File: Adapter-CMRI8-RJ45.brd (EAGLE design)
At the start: 30.9 x 38.3 mm, 6 parts

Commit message: 2.0
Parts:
- added CON1: (no value), SPCoast:1X08_LOCK
- moved J2 0.63 mm to (27.7, 11.9)
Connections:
- removed net N$17: J1.1, J2.1, J3.1
- removed net N$18: J1.2, J2.2, J3.2
- removed net N$19: J1.3, J2.3, J3.3
- removed net N$2: JP1.1, JP2.1
- removed net N$20: J1.4, J2.4, J3.4
- removed net N$21: J1.5, J2.5, J3.5
- removed net N$22: J1.6, J2.6, J3.6
- removed net N$23: J1.7, J2.7, J3.7
- removed net N$24: J1.8, J2.8, J3.8
- removed net N$3: JP1.2, JP2.2
- new net GND: JP1.1, JP1.2, JP2.1, JP2.2
- new net L1: CON1.1, J1.1, J2.1, J3.1
- new net L2: CON1.2, J1.2, J2.2, J3.2
- new net L3: CON1.3, J1.3, J2.3, J3.3
- new net L4: CON1.4, J1.4, J2.4, J3.4
- new net L5: CON1.5, J1.5, J2.5, J3.5
- new net L6: CON1.6, J1.6, J2.6, J3.6
- new net L7: CON1.7, J1.7, J2.7, J3.7
- new net L8: CON1.8, J1.8, J2.8, J3.8
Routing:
- net N$3: track 28.8 -> 0.00 mm
- net N$2: track 28.8 -> 0.00 mm
- net N$17: track 22.9 -> 0.00 mm
- net L1: track 0.00 -> 21.4 mm
- net N$23: track 21.1 -> 0.00 mm
- net N$19: track 20.2 -> 0.00 mm
- net L7: track 0.00 -> 20.1 mm
- net N$24: track 19.9 -> 0.00 mm
- net L3: track 0.00 -> 18.9 mm
- net L8: track 0.00 -> 18.9 mm
- net N$21: track 18.9 -> 0.00 mm
- net N$18: track 18.4 -> 0.00 mm
- net L5: track 0.00 -> 17.9 mm
- net L2: track 0.00 -> 17.5 mm
- net N$22: track 17.2 -> 0.00 mm
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- added copper zone on layer 16, net GND
- removed copper zone on layer 16, net N$1
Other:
- board text added: "0.100"
- board text added: "0.156"
- board text added: "2017.04"
- board text added: "3.5mm"
- board text added: "GND"
- board text added: "SPCoast"
- board text added: "v2.0"
- board text removed: "-or-"
- board text removed: "2011-10"
- board text removed: "D35725"
- board text removed: "v1.0"

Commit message: 3.0
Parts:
- removed JP1, JP2: (no value), SparkFun:SCREWTERMINAL-3.5MM-2_LOCK
- J1: value (none) -> RJ45; device con-amp:215877-7 -> SPCoast:RJ45-NO-SHIELD
- J2: device SparkFun:SCREWTERMINAL-3.5MM-8 -> SPCoast:SCREWTERMINAL-3.5MM-8
- J3: device con-molex:KK-156-8 -> SPCoast:KK-156-8-F
- moved J1 2.54 mm to (15.3, 34.2)
- moved U$1 2.54 mm to (15.2, 36.8)
- moved J3 1.27 mm to (15.6, 6.35)
- moved CON1 1.27 mm to (24.8, 15.9)
- moved J2 0.63 mm to (27.7, 12.6)
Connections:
- removed net GND: JP1.1, JP1.2, JP2.1, JP2.2
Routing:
- net L4: track 15.6 -> 19.4 mm
- net L5: track 17.9 -> 21.7 mm
- net L3: track 18.9 -> 22.7 mm
- net L6: track 16.3 -> 20.0 mm
- net L2: track 17.5 -> 21.1 mm
- net L7: track 20.1 -> 23.7 mm
- net L1: track 21.4 -> 24.9 mm
- net L8: track 18.9 -> 22.4 mm
- removed copper zone on layer 16, net GND
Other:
- board size 30.9 x 38.3 mm -> 30.9 x 39.5 mm
- board text added: "1"
- board text added: "2017.11"
- board text added: "8"
- board text added: "RJ45"
- board text added: "v3.0"
- board text removed: "2017.04"
- board text removed: "CMRI"
- board text removed: "GND"
- board text removed: "v2.0"

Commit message: 4.0
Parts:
- removed CON1: (no value), SPCoast:1X08_LOCK
- added J4: (no value), SPCoast:SCREWTERMINAL-3.5MM-4_LOCK
- added J5: (no value), SPCoast:1X08_LOCK
- added M1, M2: MOUNTINGHOLE, SPCoast:MOUNTINGHOLE
- added R1, R2, R3, R4, R5, R6, R7, R8: (no value), SPCoast:AXIAL-0.4-RES
- U$1: value OSHW-LOGOM -> DOC-OSHW-LOGO-M; device SparkFun:OSHW-LOGO-M -> SPCoast:OSHW-LOGO-M
- moved J1 11.8 mm to (15.5, 46.0)
- moved U$1 9.25 mm to (16.5, 46.0)
- moved J2 1.91 mm to (27.7, 10.7)
- moved J3 0.12 mm to (15.5, 6.35)
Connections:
- new net GND: J4.1, J4.2, J4.3, J4.4
- net L1: now also J5.1, R1.P$1, R1.P$2; no longer CON1.1
- net L2: now also J5.2, R2.P$1, R2.P$2; no longer CON1.2
- net L3: now also J5.3, R3.P$1, R3.P$2; no longer CON1.3
- net L4: now also J5.4, R4.P$1, R4.P$2; no longer CON1.4
- net L5: now also J5.5, R5.P$1, R5.P$2; no longer CON1.5
- net L6: now also J5.6, R6.P$1, R6.P$2; no longer CON1.6
- net L7: now also J5.7, R7.P$1, R7.P$2; no longer CON1.7
- net L8: now also J5.8, R8.P$1, R8.P$2; no longer CON1.8
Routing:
- net L1: track 24.9 -> 38.5 mm
- net L8: track 22.4 -> 35.8 mm
- net L3: track 22.7 -> 35.7 mm
- net L2: track 21.1 -> 33.8 mm
- net L7: track 23.7 -> 36.3 mm
- net L6: track 20.0 -> 32.4 mm
- net L5: track 21.7 -> 34.0 mm
- net L4: track 19.4 -> 31.6 mm
- net GND: track 0.00 -> 10.9 mm
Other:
- board size 30.9 x 39.5 mm -> 31 x 50 mm
- board text added: "0.156""
- board text added: "2018.12"
- board text added: "COMMON"
- board text added: "Cut on reverse for Resistors"
- board text added: "J1"
- board text added: "J2"
- board text added: "J3"
- board text added: "J4"
- board text added: "J5"
- board text added: "MRCS"
- board text added: "R1"
- board text added: "R2"
- board text added: "R3"
- board text added: "R4"
- board text added: "R5"
- board text added: "R6"
- board text added: "R7"
- board text added: "R8"
- board text added: "Resistor"
- board text added: "Tie points"
- board text added: "v4.0"
- board text added: "www . SPCoast . com"
- board text removed: ".com"
- board text removed: "2017.11"
- board text removed: "Lines"
- board text removed: "SP Coast"
- board text removed: "Shore"
- board text removed: "South"
- board text removed: "v3.0"
- board text removed: "www."

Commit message: Addrd SPDT frog power connector
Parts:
- added CON1: CONNECTOR-M033.5MM-LOCK, SPCoast:SCREWTERMINAL-3.5MM-3_LOCK.007S
- U$1: value DOC-OSHW-LOGO-M -> DOC-OSHW-LOGO-L; device SPCoast:OSHW-LOGO-M -> SPCoast:OSHW-LOGO-L
- moved M1 30.2 mm to (15.2, 46.0)
- moved J4 26.4 mm to (27.9, 36.6), turned to 90 degrees
- moved U$1 1.27 mm to (15.2, 46.0)
- moved M2 0.63 mm to (27.3, 18.7)
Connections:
- net L5: now also CON1.1
- net L6: now also CON1.2
- net L7: now also CON1.3
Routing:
- net L5: track 34.0 -> 78.7 mm
- net L6: track 32.4 -> 72.4 mm
- net L7: track 36.3 -> 67.1 mm
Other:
- board text added: "2020.06"
- board text added: "C nc no"
- board text added: "Frog Pwr"
- board text added: "no nc C"
- board text removed: "0.156""
- board text removed: "2018.12"
- board text removed: "Resistor"

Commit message: V5.0 added SPDT frog power
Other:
- board text added: "CON1"
- board text added: "v5.0"
- board text removed: "v4.0"

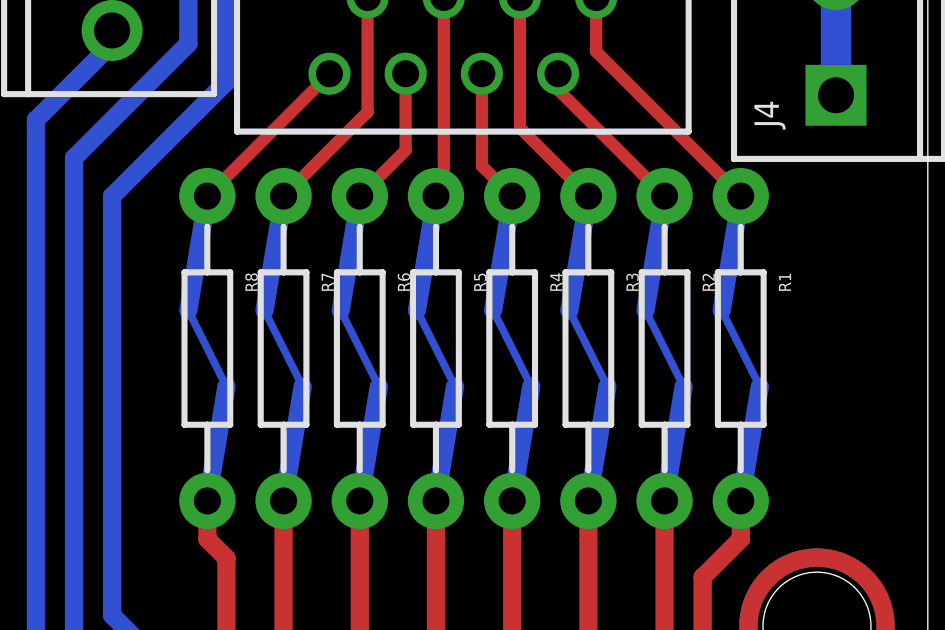
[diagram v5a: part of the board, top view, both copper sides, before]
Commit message: added values for connectors
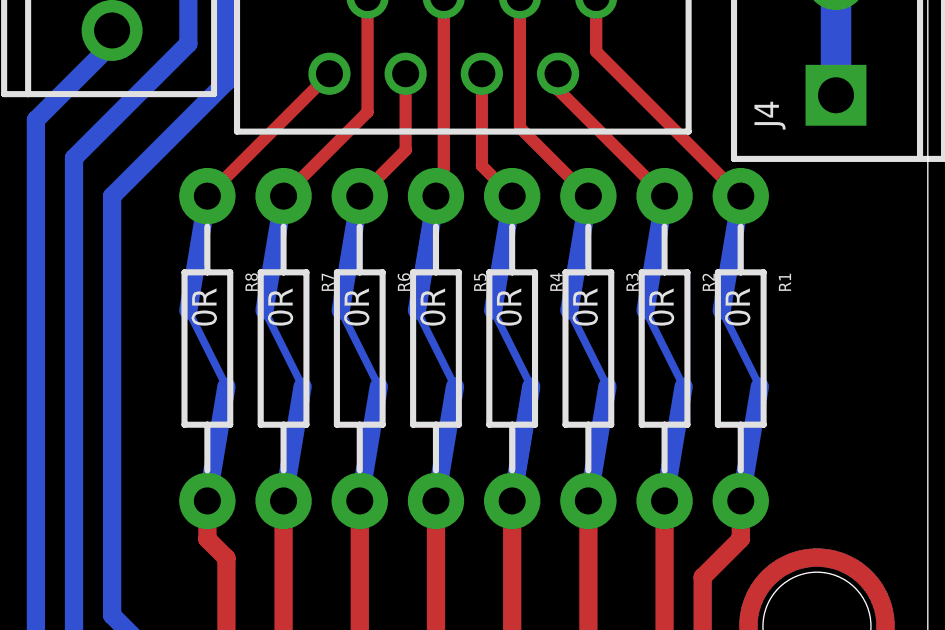
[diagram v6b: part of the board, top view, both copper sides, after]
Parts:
- J2, J4: value (none) -> 3.5mm
- J5: value (none) -> 0.100
- R1, R2, R3, R4, R5, R6, R7, R8: value (none) -> 0R
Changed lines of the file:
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@@
 <attribute name="OC_NEWARK" value="unknown" x="15.5" y="6.35" size="1.778" layer="27" rot="R180" display="off"/>
 </element>
-<element name="J2" library="SPCoast" package="SCREWTERMINAL-3.5MM-8" value="" x="27.686" y="10.668" smashed="yes" rot="R180">
+<element name="J2" library="SPCoast" package="SCREWTERMINAL-3.5MM-8" value="3.5mm" x="27.686" y="10.668" smashed="yes" rot="R180">
 <attribute name="NAME" x="27.559" y="12.446" size="0.8128" layer="25" font="vector"/>
 <attribute name="VALUE" x="28.956" y="9.398" size="0.4064" layer="27" rot="R180"/>
@@
 <attribute name="VALUE" x="18.675" y="43.45" size="1.778" layer="27" font="vector" rot="R180"/>
 </element>
-<element name="J4" library="SPCoast" package="SCREWTERMINAL-3.5MM-4_LOCK" value="" x="27.94" y="36.56" smashed="yes" rot="R90">
+<element name="J4" library="SPCoast" package="SCREWTERMINAL-3.5MM-4_LOCK" value="3.5mm" x="27.94" y="36.56" smashed="yes" rot="R90">
 <attribute name="NAME" x="26.035" y="35.29" size="0.8128" layer="25" font="vector" rot="R90"/>
 <attribute name="VALUE" x="26.67" y="35.29" size="0.4064" layer="27" rot="R90"/>
@@
 <element name="M1" library="SPCoast" package="MOUNTINGHOLE" value="MOUNTINGHOLE" x="15.24" y="45.99"/>
 <element name="M2" library="SPCoast" package="MOUNTINGHOLE" value="MOUNTINGHOLE" x="27.305" y="18.685"/>
-<element name="J5" library="SPCoast" package="1X08_LOCK" value="" x="24.765" y="13.335" rot="R180"/>
-<element name="R1" library="SPCoast" package="AXIAL-0.4-RES" value="" x="24.765" y="27.94" rot="R270"/>
-<element name="R2" library="SPCoast" package="AXIAL-0.4-RES" value="" x="22.225" y="27.94" rot="R270"/>
-<element name="R3" library="SPCoast" package="AXIAL-0.4-RES" value="" x="19.685" y="27.94" rot="R270"/>
-<element name="R4" library="SPCoast" package="AXIAL-0.4-RES" value="" x="17.145" y="27.94" rot="R270"/>
-<element name="R5" library="SPCoast" package="AXIAL-0.4-RES" value="" x="14.605" y="27.94" rot="R270"/>
-<element name="R6" library="SPCoast" package="AXIAL-0.4-RES" value="" x="12.065" y="27.94" rot="R270"/>
-<element name="R7" library="SPCoast" package="AXIAL-0.4-RES" value="" x="9.525" y="27.94" rot="R270"/>
-<element name="R8" library="SPCoast" package="AXIAL-0.4-RES" value="" x="6.985" y="27.94" rot="R270"/>
+<element name="J5" library="SPCoast" package="1X08_LOCK" value="0.100" x="24.765" y="13.335" rot="R180"/>
+<element name="R1" library="SPCoast" package="AXIAL-0.4-RES" value="0R" x="24.765" y="27.94" rot="R270"/>
+<element name="R2" library="SPCoast" package="AXIAL-0.4-RES" value="0R" x="22.225" y="27.94" rot="R270"/>
+<element name="R3" library="SPCoast" package="AXIAL-0.4-RES" value="0R" x="19.685" y="27.94" rot="R270"/>
+<element name="R4" library="SPCoast" package="AXIAL-0.4-RES" value="0R" x="17.145" y="27.94" rot="R270"/>
+<element name="R5" library="SPCoast" package="AXIAL-0.4-RES" value="0R" x="14.605" y="27.94" rot="R270"/>
+<element name="R6" library="SPCoast" package="AXIAL-0.4-RES" value="0R" x="12.065" y="27.94" rot="R270"/>
+<element name="R7" library="SPCoast" package="AXIAL-0.4-RES" value="0R" x="9.525" y="27.94" rot="R270"/>
+<element name="R8" library="SPCoast" package="AXIAL-0.4-RES" value="0R" x="6.985" y="27.94" rot="R270"/>
 <element name="CON1" library="SPCoast" package="SCREWTERMINAL-3.5MM-3_LOCK.007S" value="CONNECTOR-M033.5MM-LOCK" x="3.81" y="45.72" rot="R270"/>
 </elements>

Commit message: added values for connectors
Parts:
- J3: value (none) -> 0.156
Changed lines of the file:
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@@
 </autorouter>
 <elements>
-<element name="J3" library="SPCoast" package="KK-156-8-F" value="" x="15.5" y="6.35" smashed="yes" rot="R180">
+<element name="J3" library="SPCoast" package="KK-156-8-F" value="0.156" x="15.5" y="6.35" smashed="yes" rot="R180">
 <attribute name="NAME" x="26.676" y="8.359" size="0.8128" layer="25" font="vector"/>
 <attribute name="VALUE" x="-2.13" y="10.795" size="1.27" layer="27" rot="R270"/>

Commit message: normalized values
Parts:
- CON1: value CONNECTOR-M033.5MM-LOCK -> 3.5MM
- U$1: value DOC-OSHW-LOGO-L -> OSHW
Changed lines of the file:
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@@
 <attribute name="VALUE" x="28.956" y="9.398" size="0.4064" layer="27" rot="R180"/>
 </element>
-<element name="U$1" library="SPCoast" package="OSHW-LOGO-L" value="DOC-OSHW-LOGO-L" x="15.24" y="45.99"/>
+<element name="U$1" library="SPCoast" package="OSHW-LOGO-L" value="OSHW" x="15.24" y="45.99"/>
 <element name="J1" library="SPCoast" package="RJ45-NO-SHIELD" value="RJ45" x="15.5" y="45.99" smashed="yes" rot="R180">
 <attribute name="AMP" value="520151-4" x="15.5" y="45.99" size="1.016" layer="27" rot="R180" display="off"/>
@@
 <element name="R7" library="SPCoast" package="AXIAL-0.4-RES" value="0R" x="9.525" y="27.94" rot="R270"/>
 <element name="R8" library="SPCoast" package="AXIAL-0.4-RES" value="0R" x="6.985" y="27.94" rot="R270"/>
-<element name="CON1" library="SPCoast" package="SCREWTERMINAL-3.5MM-3_LOCK.007S" value="CONNECTOR-M033.5MM-LOCK" x="3.81" y="45.72" rot="R270"/>
+<element name="CON1" library="SPCoast" package="SCREWTERMINAL-3.5MM-3_LOCK.007S" value="3.5MM" x="3.81" y="45.72" rot="R270"/>
 </elements>
 <signals>
